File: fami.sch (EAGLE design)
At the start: 14 parts, among them IC1 PROM, IC2 WRAM, IC3 CHROM, IC4 74LS20N

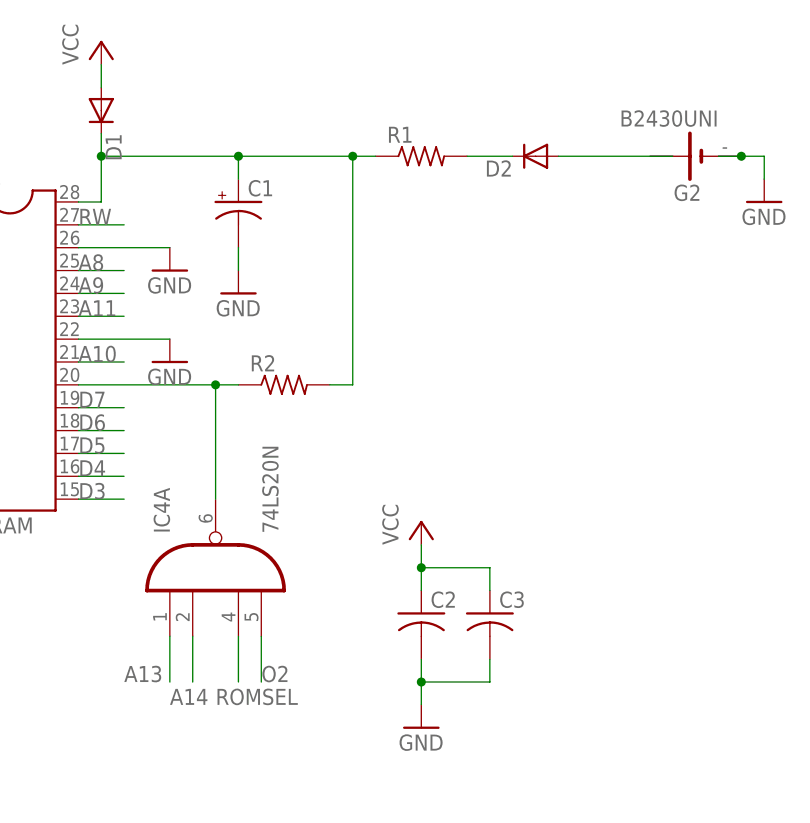
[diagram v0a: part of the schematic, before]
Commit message: Added R and C values
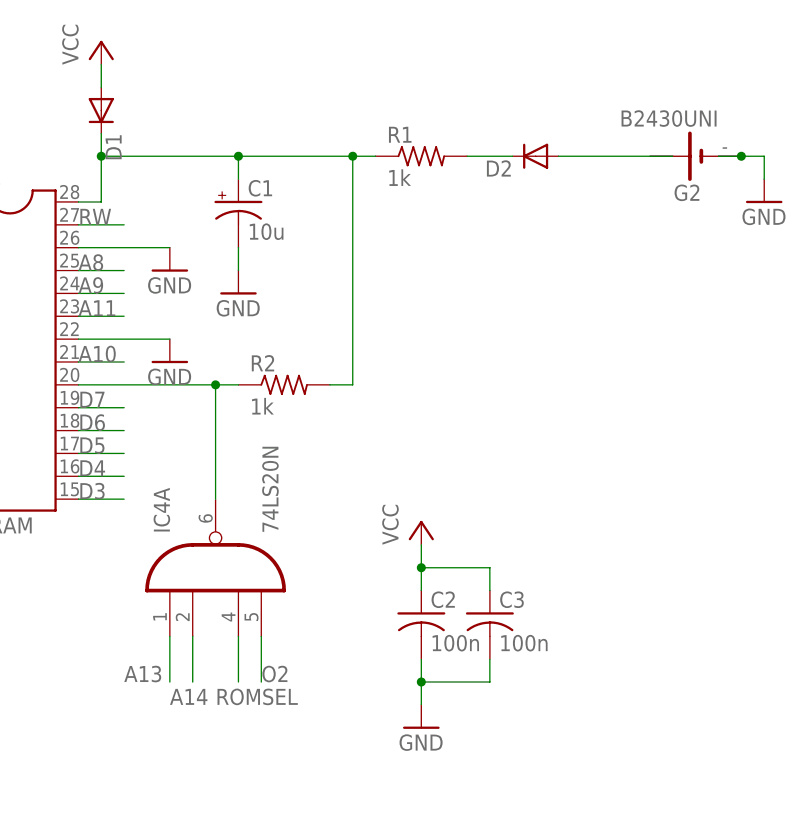
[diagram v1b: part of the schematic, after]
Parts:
- C1: value (none) -> 10u
- C2, C3: value (none) -> 100n
- R1, R2: value (none) -> 1k
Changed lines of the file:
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@@
 <part name="GND10" library="supply1" deviceset="GND" device=""/>
 <part name="GND11" library="supply1" deviceset="GND" device=""/>
-<part name="C1" library="rcl" deviceset="CPOL-US" device="E2.5-6"/>
-<part name="C2" library="rcl" deviceset="C-US" device="025-025X050"/>
-<part name="R1" library="rcl" deviceset="R-US_" device="0204/7"/>
+<part name="C1" library="rcl" deviceset="CPOL-US" device="E2.5-6" value="10u"/>
+<part name="C2" library="rcl" deviceset="C-US" device="025-025X050" value="100n"/>
+<part name="R1" library="rcl" deviceset="R-US_" device="0204/7" value="1k"/>
 <part name="P+6" library="supply1" deviceset="VCC" device=""/>
 <part name="GND12" library="supply1" deviceset="GND" device=""/>
-<part name="R2" library="rcl" deviceset="R-US_" device="0204/7"/>
+<part name="R2" library="rcl" deviceset="R-US_" device="0204/7" value="1k"/>
 <part name="GND13" library="supply1" deviceset="GND" device=""/>
-<part name="C3" library="rcl" deviceset="C-US" device="025-025X050"/>
+<part name="C3" library="rcl" deviceset="C-US" device="025-025X050" value="100n"/>
 <part name="G2" library="battery" deviceset="B2430UNI" device=""/>
 </parts>

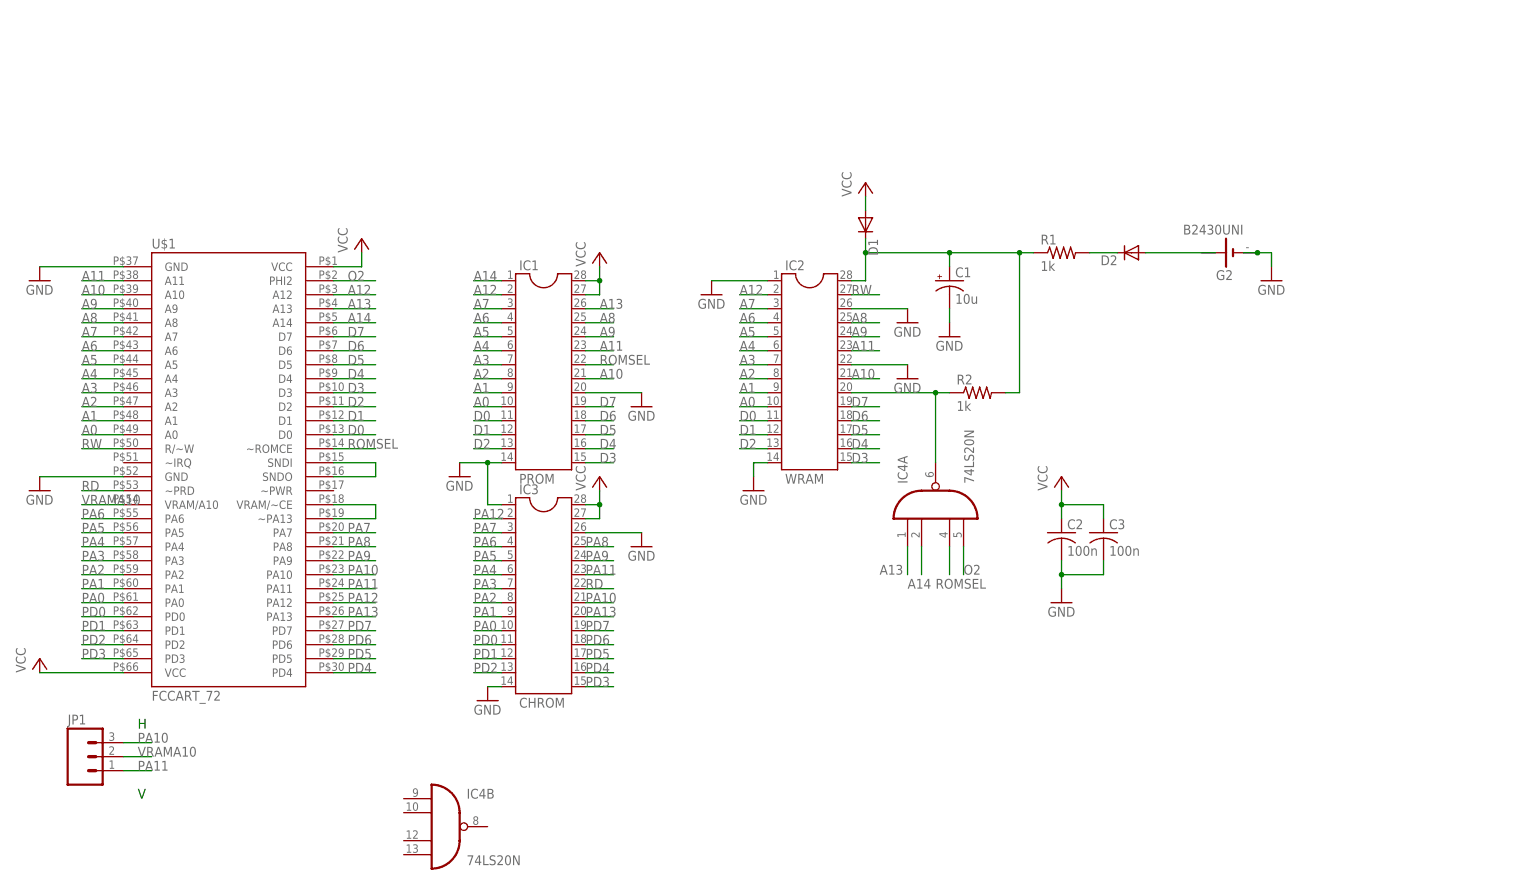
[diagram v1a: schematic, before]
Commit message: Added support for CNROM and GNROM
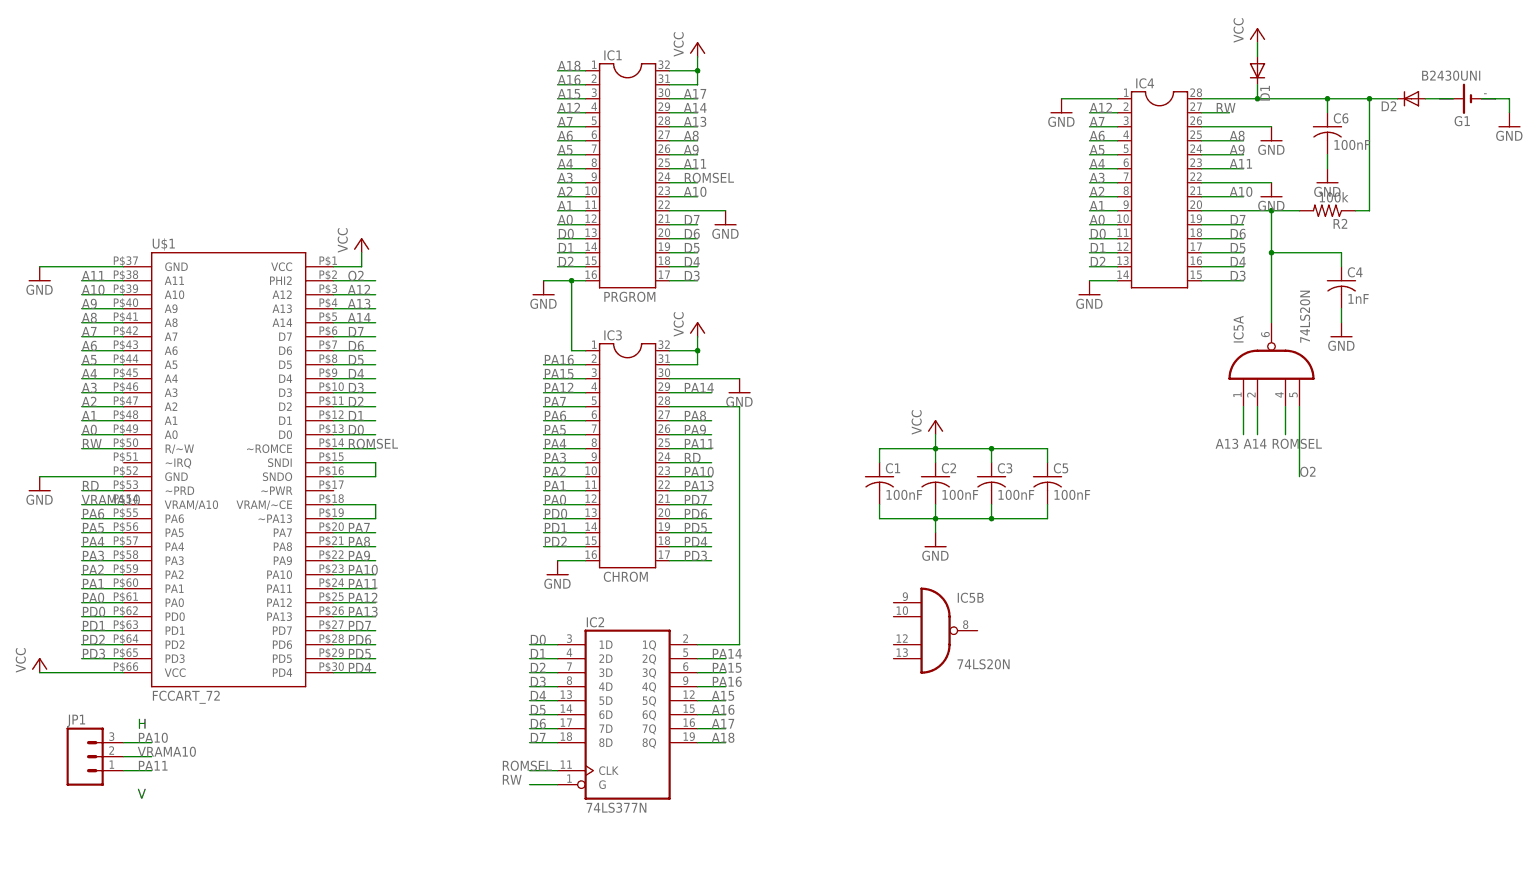
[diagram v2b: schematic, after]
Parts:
- removed G2: B2430UNI, battery:B2430UNI
- removed R1: 1k, rcl:R-US_0204/7
- added C4: 1nF, rcl:C-US025-025X050
- added C5, C6: 100nF, rcl:C-US025-025X050
- added G1: B2430UNI, battery:B2430UNI
- added IC5: 74LS20N, 74xx-eu:74LS20N
- C1: value 10u -> 100nF; device rcl:CPOL-USE2.5-6 -> rcl:C-US025-025X050
- C2, C3: value 100n -> 100nF
- IC1: value PROM -> PRGROM; device ic-package:DIL28 -> ic-package:DIL32
- IC2: value WRAM -> 74LS377N; device ic-package:DIL28 -> 74xx-us:74LS377N
- IC3: device ic-package:DIL28 -> ic-package:DIL32
- IC4: value 74LS20N -> (none); device 74xx-eu:74LS20N -> ic-package:DIL28
- R2: value 1k -> 100k
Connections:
- removed net N$24: C1.+, D1.C, IC2.28, R1.1, R2.2
- removed net N$4: D2.A, G2.+@4
- new net A15: IC1.3, IC2A.5Q
- new net A16: IC1.2, IC2A.6Q
- new net A17: IC1.30, IC2A.7Q
- new net A18: IC1.1, IC2A.8Q
- new net N$7: C4.1, IC4.20, IC5A.O, R2.2
- new net N$9: D2.A, G1.+@4
- new net PA14: IC2A.2Q, IC3.29
- new net PA15: IC2A.3Q, IC3.3
- new net PA16: IC2A.4Q, IC3.2
- net A0: now also IC1.12, IC4.10; no longer IC1.10, IC2.10
- net A1: now also IC1.11, IC4.9; no longer IC1.9, IC2.9
- net A10: now also IC1.23, IC4.21; no longer IC1.21, IC2.21
- net A11: now also IC1.25, IC4.23; no longer IC1.23, IC2.23
- net A12: now also IC1.4, IC4.2; no longer IC1.2, IC2.2
- net A13: now also IC1.28, IC5A.I0; no longer IC1.26, IC4A.I0
- net A14: now also IC1.29, IC5A.I1; no longer IC1.1, IC4A.I1
- net A2: now also IC1.10, IC4.8; no longer IC1.8, IC2.8
- net A3: now also IC1.9, IC4.7; no longer IC1.7, IC2.7
- net A4: now also IC1.8, IC4.6; no longer IC1.6, IC2.6
- net A5: now also IC1.7, IC4.5; no longer IC1.5, IC2.5
- net A6: now also IC1.6, IC4.4; no longer IC1.4, IC2.4
- net A7: now also IC1.5, IC4.3; no longer IC1.3, IC2.3
- net A8: now also IC1.27, IC4.25; no longer IC1.25, IC2.25
- net A9: now also IC1.26, IC4.24; no longer IC1.24, IC2.24
- net D0: now also IC1.13, IC2A.1D, IC4.11; no longer IC1.11, IC2.11
- net D1: now also IC1.14, IC2A.2D, IC4.12; no longer IC1.12, IC2.12
- net D2: now also IC1.15, IC2A.3D, IC4.13; no longer IC1.13, IC2.13
- net D3: now also IC1.17, IC2A.4D, IC4.15; no longer IC1.15, IC2.15
- net D4: now also IC1.18, IC2A.5D, IC4.16; no longer IC1.16, IC2.16
- net D5: now also IC1.19, IC2A.6D, IC4.17; no longer IC1.17, IC2.17
- net D6: now also IC1.20, IC2A.7D, IC4.18; no longer IC1.18, IC2.18
- net D7: now also IC1.21, IC2A.8D, IC4.19; no longer IC1.19, IC2.19
- net GND: now also C1.2, C4.2, C5.2, C6.2, G1.-, G1.-@1, IC1.16, IC1.22, IC3.16, IC3.30, IC4.1, IC4.14, IC4.22, IC4.26; no longer C1.-, G2.-, G2.-@1, IC1.14, IC1.20, IC2.1, IC2.14, IC2.22, IC2.26, IC3.14, IC3.26
- net N$1: now also IC2A.1Q, IC3.28; no longer D2.C, R1.2
- net N$6: now also C6.1, D1.C, D2.C, IC4.28; no longer IC2.20, IC4A.O
- net O2: now also IC5A.I3; no longer IC4A.I3
- net PA0: now also IC3.12; no longer IC3.10
- net PA1: now also IC3.11; no longer IC3.9
- net PA10: now also IC3.23; no longer IC3.21
- net PA11: now also IC3.25; no longer IC3.23
- net PA12: now also IC3.4; no longer IC3.2
- net PA13: now also IC3.22; no longer IC3.20
- net PA2: now also IC3.10; no longer IC3.8
- net PA3: now also IC3.9; no longer IC3.7
- net PA4: now also IC3.8; no longer IC3.6
- net PA5: now also IC3.7; no longer IC3.5
- net PA6: now also IC3.6; no longer IC3.4
- net PA7: now also IC3.5; no longer IC3.3
- net PA8: now also IC3.27; no longer IC3.25
- net PA9: now also IC3.26; no longer IC3.24
- net PD0: now also IC3.13; no longer IC3.11
- net PD1: now also IC3.14; no longer IC3.12
- net PD2: now also IC3.15; no longer IC3.13
- net PD3: now also IC3.17; no longer IC3.15
- net PD4: now also IC3.18; no longer IC3.16
- net PD5: now also IC3.19; no longer IC3.17
- net PD6: now also IC3.20; no longer IC3.18
- net PD7: now also IC3.21; no longer IC3.19
- net RD: now also IC3.24; no longer IC3.22
- net ROMSEL: now also IC1.24, IC2A.CLK, IC5A.I2; no longer IC1.22, IC4A.I2
- net RW: now also IC2A.G, IC4.27; no longer IC2.27
- net VCC: now also C1.1, C5.1, IC1.31, IC1.32, IC3.31, IC3.32; no longer IC1.27, IC1.28, IC3.27, IC3.28
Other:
- moved on the sheet: C2, C3, D1, D2, R2
